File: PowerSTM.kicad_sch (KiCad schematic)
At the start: 1 part, among them IC2 TCAN3414DRBR

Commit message: WIFI connection changes PI
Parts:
- removed IC2: TCAN3414DRBR, dz_comm_TCAN3414DRBR, symbol #dzdb:s_comm/COMM-TI-TCAN3414DRBR
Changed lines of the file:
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@@
 	(generator_version "9.0")
 	(paper "A4")
-	(symbol
-		(lib_id "#dzdb:s_comm/COMM-TI-TCAN3414DRBR")
-		(at 106.68 77.47 0)
-		(unit 1)
-		(exclude_from_sim no)
-		(in_bom yes)
-		(on_board yes)
-		(dnp no)
-		(fields_autoplaced yes)
-		(property "Reference" "IC2"
-			(at 121.92 69.85 0)
-			(effects
-				(font
-					(size 1.27 1.27)
-				)
-			)
-		)
-		(property "Value" "TCAN3414DRBR"
-			(at 121.92 72.39 0)
-			(effects
-				(font
-					(size 1.27 1.27)
-				)
-			)
-		)
-		(property "Footprint" "dz_comm_TCAN3414DRBR"
-			(at 133.35 172.39 0)
-			(effects
-				(font
-					(size 1.27 1.27)
-				)
-				(justify left top)
-				(hide yes)
-			)
-		)
-		(property "Datasheet" "https://www.ti.com/lit/gpn/tcan3414"
-			(at 133.35 272.39 0)
-			(effects
-				(font
-					(size 1.27 1.27)
-				)
-				(justify left top)
-				(hide yes)
-			)
-		)
-		(property "Description" "CAN Interface IC CAN FD Transceiver with Integrated Controller"
-			(at 106.68 77.47 0)
-			(effects
-				(font
-					(size 1.27 1.27)
-				)
-				(hide yes)
-			)
-		)
-		(property "Height" "1"
-			(at 133.35 472.39 0)
-			(effects
-				(font
-					(size 1.27 1.27)
-				)
-				(justify left top)
-				(hide yes)
-			)
-		)
-		(property "Mouser Part Number" "595-TCAN3414DRBR"
-			(at 133.35 572.39 0)
-			(effects
-				(font
-					(size 1.27 1.27)
-				)
-				(justify left top)
-				(hide yes)
-			)
-		)
-		(property "Mouser Price/Stock" "https://www.mouser.co.uk/ProductDetail/Texas-Instruments/TCAN3414DRBR?qs=2wMNvWM5ZX6YBBH9qF6w4g%3D%3D"
-			(at 133.35 672.39 0)
-			(effects
-				(font
-					(size 1.27 1.27)
-				)
-				(justify left top)
-				(hide yes)
-			)
-		)
-		(property "Manufacturer_Name" "Texas Instruments"
-			(at 133.35 772.39 0)
-			(effects
-				(font
-					(size 1.27 1.27)
-				)
-				(justify left top)
-				(hide yes)
-			)
-		)
-		(property "Manufacturer_Part_Number" "TCAN3414DRBR"
-			(at 133.35 872.39 0)
-			(effects
-				(font
-					(size 1.27 1.27)
-				)
-				(justify left top)
-				(hide yes)
-			)
-		)
-		(property "IPN" "COMM-TI-TCAN3414DRBR"
-			(at 106.68 77.47 0)
-			(effects
-				(font
-					(size 1.27 1.27)
-				)
-				(hide yes)
-			)
-		)
-		(property "MPN" "TCAN3414DRBR"
-			(at 106.68 77.47 0)
-			(effects
-				(font
-					(size 1.27 1.27)
-				)
-				(hide yes)
-			)
-		)
-		(property "Manufacturer" "Texas Instruments"
-			(at 106.68 77.47 0)
-			(effects
-				(font
-					(size 1.27 1.27)
-				)
-				(hide yes)
-			)
-		)
-		(property "Type" "Can Tranciever"
-			(at 106.68 77.47 0)
-			(effects
-				(font
-					(size 1.27 1.27)
-				)
-				(hide yes)
-			)
-		)
-		(property "Supply" "3V-3.3V"
-			(at 106.68 77.47 0)
-			(effects
-				(font
-					(size 1.27 1.27)
-				)
-				(hide yes)
-			)
-		)
-		(property "Package" "SON-8"
-			(at 106.68 77.47 0)
-			(effects
-				(font
-					(size 1.27 1.27)
-				)
-				(hide yes)
-			)
-		)
-		(property "Supplier" "Mouser"
-			(at 106.68 77.47 0)
-			(effects
-				(font
-					(size 1.27 1.27)
-				)
-				(hide yes)
-			)
-		)
-		(property "SPN" " 595-TCAN3414DRBR"
-			(at 106.68 77.47 0)
-			(effects
-				(font
-					(size 1.27 1.27)
-				)
-				(hide yes)
-			)
-		)
-		(property "LCSC" "Cxxxxxx"
-			(at 106.68 77.47 0)
-			(effects
-				(font
-					(size 1.27 1.27)
-				)
-				(hide yes)
-			)
-		)
-		(property "Comment" ""
-			(at 106.68 77.47 0)
-			(effects
-				(font
-					(size 1.27 1.27)
-				)
-				(hide yes)
-			)
-		)
-		(pin "1"
-		)
-		(pin "2"
-		)
-		(pin "3"
-		)
-		(pin "4"
-		)
-		(pin "8"
-		)
-		(pin "7"
-		)
-		(pin "6"
-		)
-		(pin "5"
-		)
-		(pin "9"
-		)
-		(instances
-			(project ""
-				(path "/ce1819b2-f280-40ed-834f-6fe4d12f809d/46fb4fb5-44f2-465b-b1ff-e4e0fbef74ae/b861b505-f377-49fb-9e06-1714af927ea6"
-					(reference "IC2")
-					(unit 1)
-				)
-			)
-		)
-	)
 )

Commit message: CAN tranciever
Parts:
- added IC2: TCAN3414DRBR, dz_comm:TCAN3414DRBR, symbol #dzdb:s_comm/COMM-TI-TCAN3414DRBR
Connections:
- new net +3.3V: IC2.3 (V_CC)
- new net FDCAN_STM_RX: IC2.1 (TXD)
- new net FDCAN_STM_TX: IC2.4 (RXD)
- new net GND: IC2.2 (GND), IC2.9 (EP)

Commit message: added caps
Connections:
- net ST_CAN_N: now reaches IC2.6 (CANL)
- net ST_CAN_P: now reaches IC2.7 (CANH)
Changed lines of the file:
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@@
+	(wire
+		(pts
+			(xy 157.48 83.82) (xy 177.8 83.82)
+		)
+		(stroke
+			(width 0)
+			(type default)
+		)
+	)
 	(wire
 		(pts
@@
 		)
 	)
+	(wire
+		(pts
+			(xy 157.48 81.28) (xy 177.8 81.28)
+		)
+		(stroke
+			(width 0)
+			(type default)
+		)
+	)
+	(label "ST_CAN_P"
+		(at 177.8 81.28 180)
+		(effects
+			(font
+				(size 1.27 1.27)
+			)
+			(justify right bottom)
+		)
+	)
+	(label "ST_CAN_N"
+		(at 177.8 83.82 180)
+		(effects
+			(font
+				(size 1.27 1.27)
+			)
+			(justify right bottom)
+		)
+	)

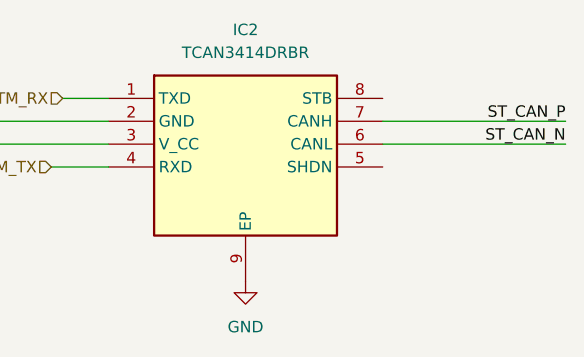
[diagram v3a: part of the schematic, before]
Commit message: added connections for can
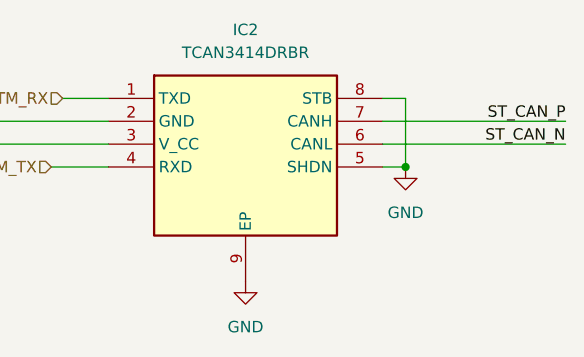
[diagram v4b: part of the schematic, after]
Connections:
- net GND: now also IC2.5 (SHDN), IC2.8 (STB)
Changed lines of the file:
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@@
 	(generator_version "9.0")
 	(paper "A4")
+	(junction
+		(at 160.02 86.36)
+		(diameter 0)
+		(color 0 0 0 0)
+	)
 	(wire
 		(pts
@@
 	(wire
 		(pts
+			(xy 160.02 86.36) (xy 157.48 86.36)
+		)
+		(stroke
+			(width 0)
+			(type default)
+		)
+	)
+	(wire
+		(pts
 			(xy 127 81.28) (xy 100.33 81.28)
 		)
@@
 		(pts
 			(xy 120.65 86.36) (xy 127 86.36)
+		)
+		(stroke
+			(width 0)
+			(type default)
+		)
+	)
+	(wire
+		(pts
+			(xy 160.02 78.74) (xy 160.02 86.36)
+		)
+		(stroke
+			(width 0)
+			(type default)
+		)
+	)
+	(wire
+		(pts
+			(xy 157.48 78.74) (xy 160.02 78.74)
 		)
 		(stroke
@@
 					(unit 1)
 				)
+			)
+		)
+	)
+	(symbol
+		(lib_id "power:GND")
+		(at 160.02 86.36 0)
+		(unit 1)
+		(exclude_from_sim no)
+		(in_bom yes)
+		(on_board yes)
+		(dnp no)
+		(fields_autoplaced yes)
+		(property "Reference" "#PWR038"
+			(at 160.02 92.71 0)
+			(effects
+				(font
+					(size 1.27 1.27)
+				)
+				(hide yes)
+			)
+		)
+		(property "Value" "GND"
+			(at 160.02 91.44 0)
+			(effects
+				(font
+					(size 1.27 1.27)
+				)
+			)
+		)
+		(property "Footprint" ""
+			(at 160.02 86.36 0)
+			(effects
+				(font
+					(size 1.27 1.27)
+				)
+				(hide yes)
+			)
+		)
+		(property "Datasheet" ""
+			(at 160.02 86.36 0)
+			(effects
+				(font
+					(size 1.27 1.27)
+				)
+				(hide yes)
+			)
+		)
+		(property "Description" "Power symbol creates a global label with name \"GND\" , ground"
+			(at 160.02 86.36 0)
+			(effects
+				(font
+					(size 1.27 1.27)
+				)
+				(hide yes)
+			)
+		)
+		(pin "1"
+		)
+		(instances
+			(project ""
+				(path "/ce1819b2-f280-40ed-834f-6fe4d12f809d/46fb4fb5-44f2-465b-b1ff-e4e0fbef74ae/b861b505-f377-49fb-9e06-1714af927ea6"
+					(reference "#PWR038")
+					(unit 1)
+				)

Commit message: Added Power logic finally. (plus some comments on further improvements)
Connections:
- net +3.3V renamed Battery_Out_3.3V
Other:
- note added: "Can only connected when battery is connected!"
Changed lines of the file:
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@@
 	(generator_version "9.0")
 	(paper "A4")
+	(text "Can only connected when battery is connected!"
+		(exclude_from_sim no)
+		(at 76.454 97.282 0)
+		(effects
+			(font
+				(size 1.27 1.27)
+			)
+		)
+	)
 	(junction
 		(at 160.02 86.36)
@@
 		(pts
 			(xy 120.65 86.36) (xy 127 86.36)
+		)
+		(stroke
+			(width 0)
+			(type default)
+		)
+	)
+	(wire
+		(pts
+			(xy 102.87 83.82) (xy 102.87 97.79)
 		)
 		(stroke
@@
 			)
 			(justify right bottom)
+		)
+	)
+	(global_label "Battery_Out_3.3V"
+		(shape input)
+		(at 102.87 97.79 270)
+		(fields_autoplaced yes)
+		(effects
+			(font
+				(size 1.27 1.27)
+			)
+			(justify right)
+		)
+		(property "Intersheetrefs" "${INTERSHEET_REFS}"
+			(at 102.87 116.7408 90)
+			(effects
+				(font
+					(size 1.27 1.27)
+				)
+				(justify right)
+				(hide yes)
+			)
 		)
 	)
@@
 		(dnp no)
 		(fields_autoplaced yes)
-		(property "Reference" "#PWR025"
+		(property "Reference" "#PWR015"
 			(at 100.33 91.44 0)
 			(effects
@@
 			(project ""
 				(path "/ce1819b2-f280-40ed-834f-6fe4d12f809d/46fb4fb5-44f2-465b-b1ff-e4e0fbef74ae/b861b505-f377-49fb-9e06-1714af927ea6"
-					(reference "#PWR025")
+					(reference "#PWR015")
 					(unit 1)
 				)
@@
 		(dnp no)
 		(fields_autoplaced yes)
-		(property "Reference" "#PWR038"
+		(property "Reference" "#PWR017"
 			(at 160.02 92.71 0)
 			(effects
@@
 			(project ""
 				(path "/ce1819b2-f280-40ed-834f-6fe4d12f809d/46fb4fb5-44f2-465b-b1ff-e4e0fbef74ae/b861b505-f377-49fb-9e06-1714af927ea6"
-					(reference "#PWR038")
+					(reference "#PWR017")
 					(unit 1)
 				)
@@
 		(dnp no)
 		(fields_autoplaced yes)
-		(property "Reference" "#PWR03"
+		(property "Reference" "#PWR016"
 			(at 142.24 105.41 0)
 			(effects
@@
 			(project ""
 				(path "/ce1819b2-f280-40ed-834f-6fe4d12f809d/46fb4fb5-44f2-465b-b1ff-e4e0fbef74ae/b861b505-f377-49fb-9e06-1714af927ea6"
-					(reference "#PWR03")
+					(reference "#PWR016")
 					(unit 1)
 				)
-			)
-		)
-	)
-	(symbol
-		(lib_id "power:+3.3V")
-		(at 102.87 83.82 0)
-		(unit 1)
-		(exclude_from_sim no)
-		(in_bom yes)
-		(on_board yes)
-		(dnp no)
-		(fields_autoplaced yes)
-		(property "Reference" "#PWR028"
-			(at 102.87 87.63 0)
-			(effects
-				(font
-					(size 1.27 1.27)
-				)
-				(hide yes)
-			)
-		)
-		(property "Value" "+3.3V"
-			(at 102.87 78.74 0)
-			(effects
-				(font
-					(size 1.27 1.27)
-				)
-			)
-		)
-		(property "Footprint" ""
-			(at 102.87 83.82 0)
-			(effects
-				(font
-					(size 1.27 1.27)
-				)
-				(hide yes)
-			)
-		)
-		(property "Datasheet" ""
-			(at 102.87 83.82 0)
-			(effects
-				(font
-					(size 1.27 1.27)
-				)
-				(hide yes)
-			)
-		)
-		(property "Description" "Power symbol creates a global label with name \"+3.3V\""
-			(at 102.87 83.82 0)
-			(effects
-				(font
-					(size 1.27 1.27)
-				)
-				(hide yes)
-			)
-		)
-		(pin "1"
-		)
-		(instances
-			(project ""
-				(path "/ce1819b2-f280-40ed-834f-6fe4d12f809d/46fb4fb5-44f2-465b-b1ff-e4e0fbef74ae/b861b505-f377-49fb-9e06-1714af927ea6"
-					(reference "#PWR028")
-					(unit 1)
-				)

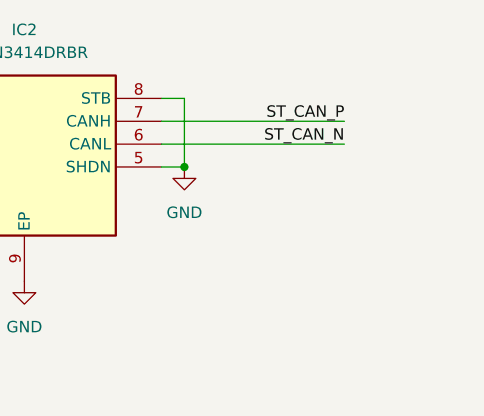
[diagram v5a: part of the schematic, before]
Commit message: routed the CAN
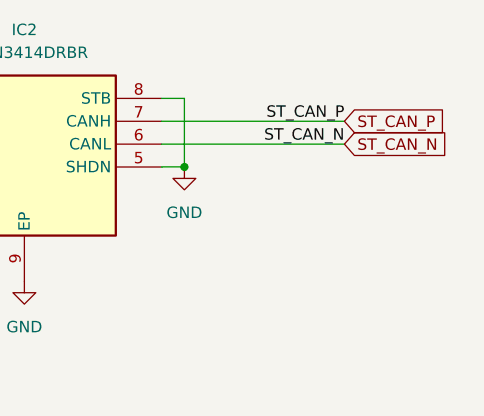
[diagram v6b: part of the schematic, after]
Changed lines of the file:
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@@
+		)
+	)
+	(global_label "ST_CAN_N"
+		(shape input)
+		(at 177.8 83.82 0)
+		(fields_autoplaced yes)
+		(effects
+			(font
+				(size 1.27 1.27)
+			)
+			(justify left)
+		)
+		(property "Intersheetrefs" "${INTERSHEET_REFS}"
+			(at 189.9171 83.82 0)
+			(effects
+				(font
+					(size 1.27 1.27)
+				)
+				(justify left)
+				(hide yes)
+			)
+		)
+	)
+	(global_label "ST_CAN_P"
+		(shape input)
+		(at 177.8 81.28 0)
+		(fields_autoplaced yes)
+		(effects
+			(font
+				(size 1.27 1.27)
+			)
+			(justify left)
+		)
+		(property "Intersheetrefs" "${INTERSHEET_REFS}"
+			(at 189.8566 81.28 0)
+			(effects
+				(font
+					(size 1.27 1.27)
+				)
+				(justify left)
+				(hide yes)
+			)
 		)
 	)

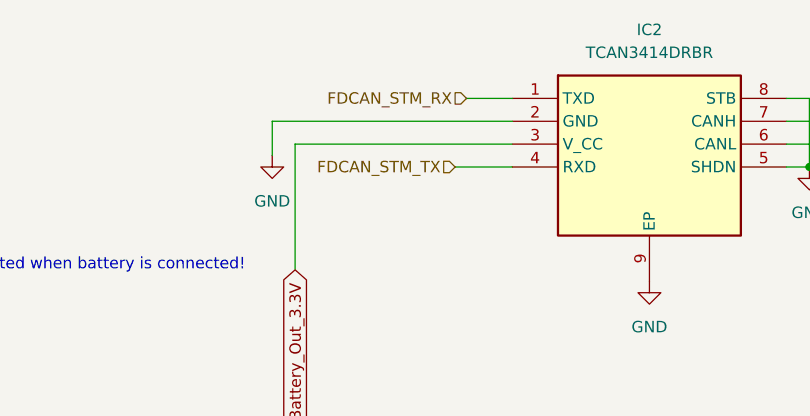
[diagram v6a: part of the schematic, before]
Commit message: added the stmv3 connector and fixed the issues
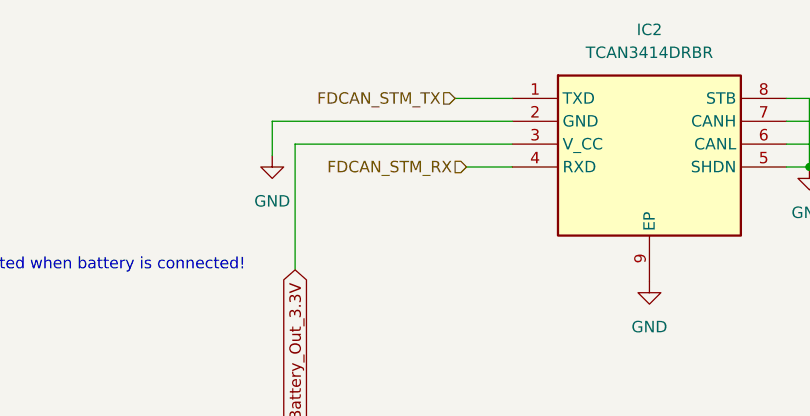
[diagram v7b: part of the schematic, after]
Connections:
- net FDCAN_STM_RX: now also IC2.4 (RXD); no longer IC2.1 (TXD)
- net FDCAN_STM_TX: now also IC2.1 (TXD); no longer IC2.4 (RXD)
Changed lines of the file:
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@@
-	(wire
-		(pts
-			(xy 121.92 78.74) (xy 127 78.74)
-		)
-		(stroke
-			(width 0)
-			(type default)
-		)
-	)
 	(wire
 		(pts
@@
 	(wire
 		(pts
+			(xy 120.65 78.74) (xy 127 78.74)
+		)
+		(stroke
+			(width 0)
+			(type default)
+		)
+	)
+	(wire
+		(pts
+			(xy 121.92 86.36) (xy 127 86.36)
+		)
+		(stroke
+			(width 0)
+			(type default)
+		)
+	)
+	(wire
+		(pts
 			(xy 127 81.28) (xy 100.33 81.28)
 		)
@@
 		(pts
 			(xy 102.87 83.82) (xy 127 83.82)
-		)
-		(stroke
-			(width 0)
-			(type default)
-		)
-	)
-	(wire
-		(pts
-			(xy 120.65 86.36) (xy 127 86.36)
 		)
 		(stroke
@@
 	(hierarchical_label "FDCAN_STM_RX"
 		(shape input)
-		(at 121.92 78.74 180)
+		(at 121.92 86.36 180)
 		(effects
 			(font
@@
 	(hierarchical_label "FDCAN_STM_TX"
 		(shape input)
-		(at 120.65 86.36 180)
+		(at 120.65 78.74 180)
 		(effects
 			(font

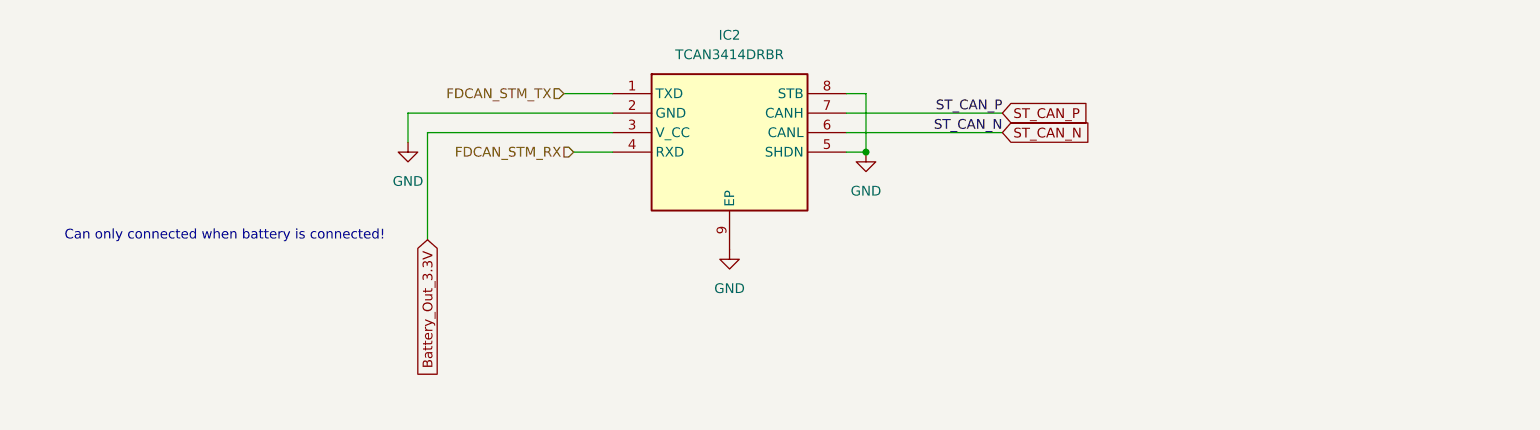
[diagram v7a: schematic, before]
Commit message: added can termination resistance and esd protection
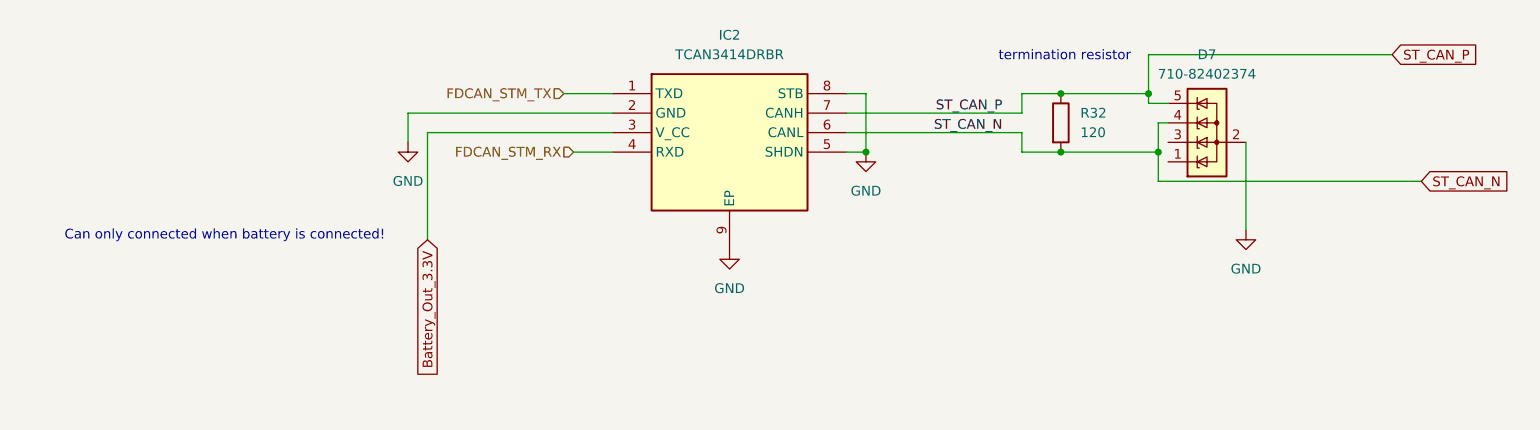
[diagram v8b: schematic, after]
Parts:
- added D7: 710-82402374, Package_TO_SOT_SMD:SOT-23-5, symbol #dzdb:s_dio/WURT-710-82402374
- added R32: 120, Resistor_SMD:R_0603_1608Metric, symbol #dzdb:g_res/R-120-0603
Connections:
- net GND: now also D7.2 (A)
- net ST_CAN_N: now also D7.4 (K), R32.2
- net ST_CAN_P: now also D7.5 (K), R32.1
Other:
- note added: "termination resistor"
